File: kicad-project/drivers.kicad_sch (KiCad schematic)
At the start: 10 parts

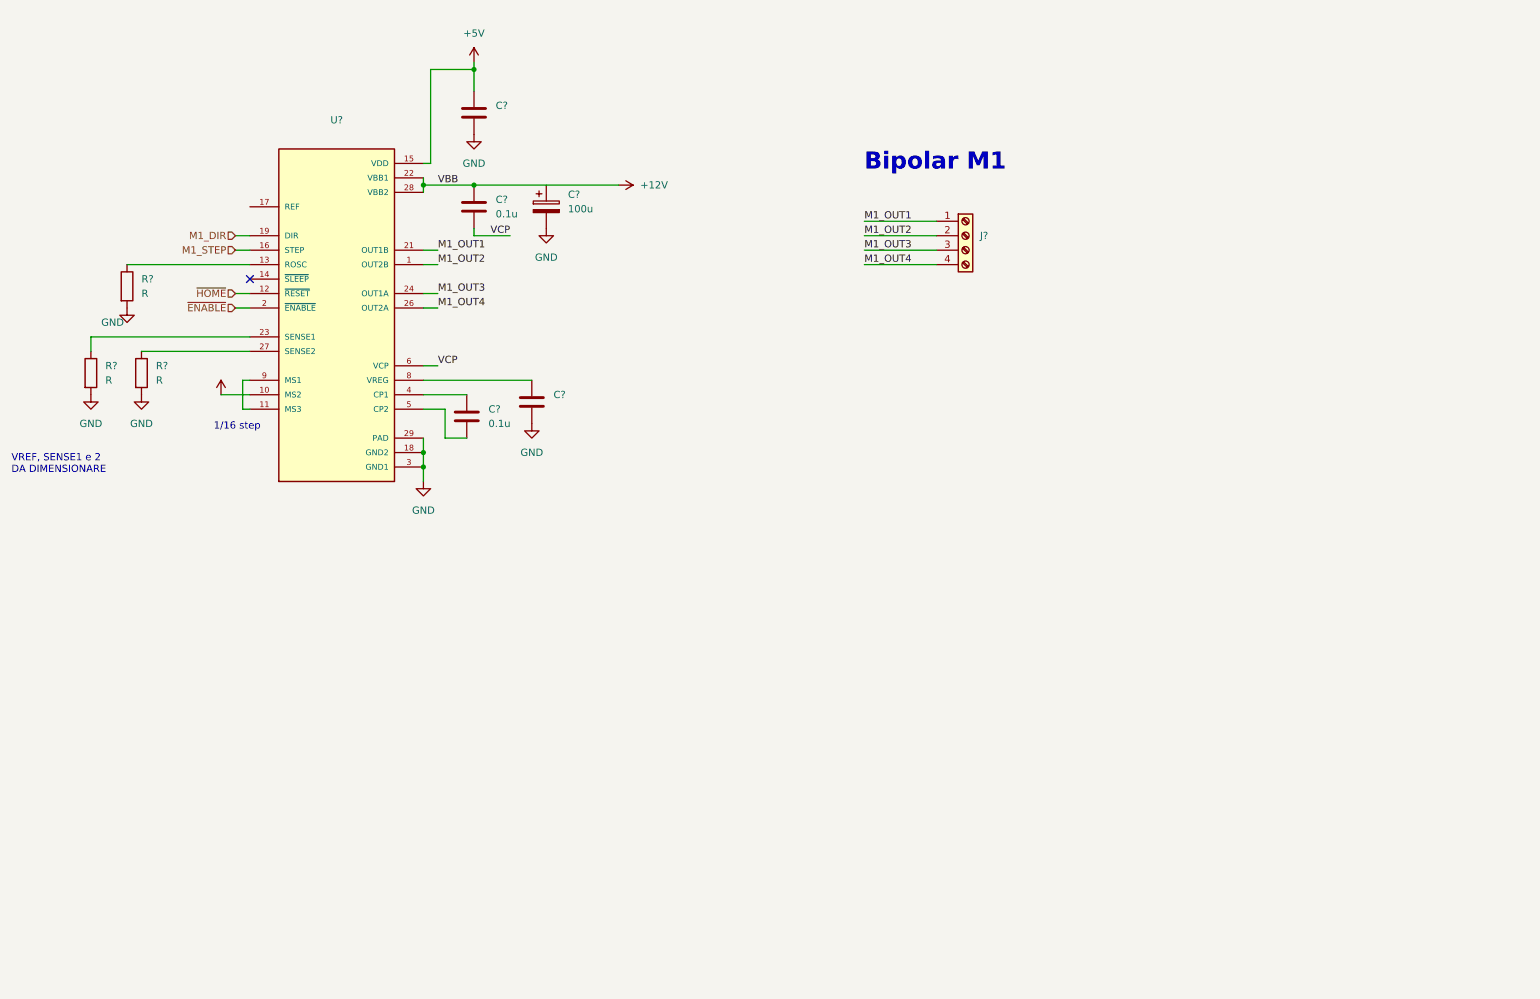
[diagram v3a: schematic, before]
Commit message: hw: add esp8266
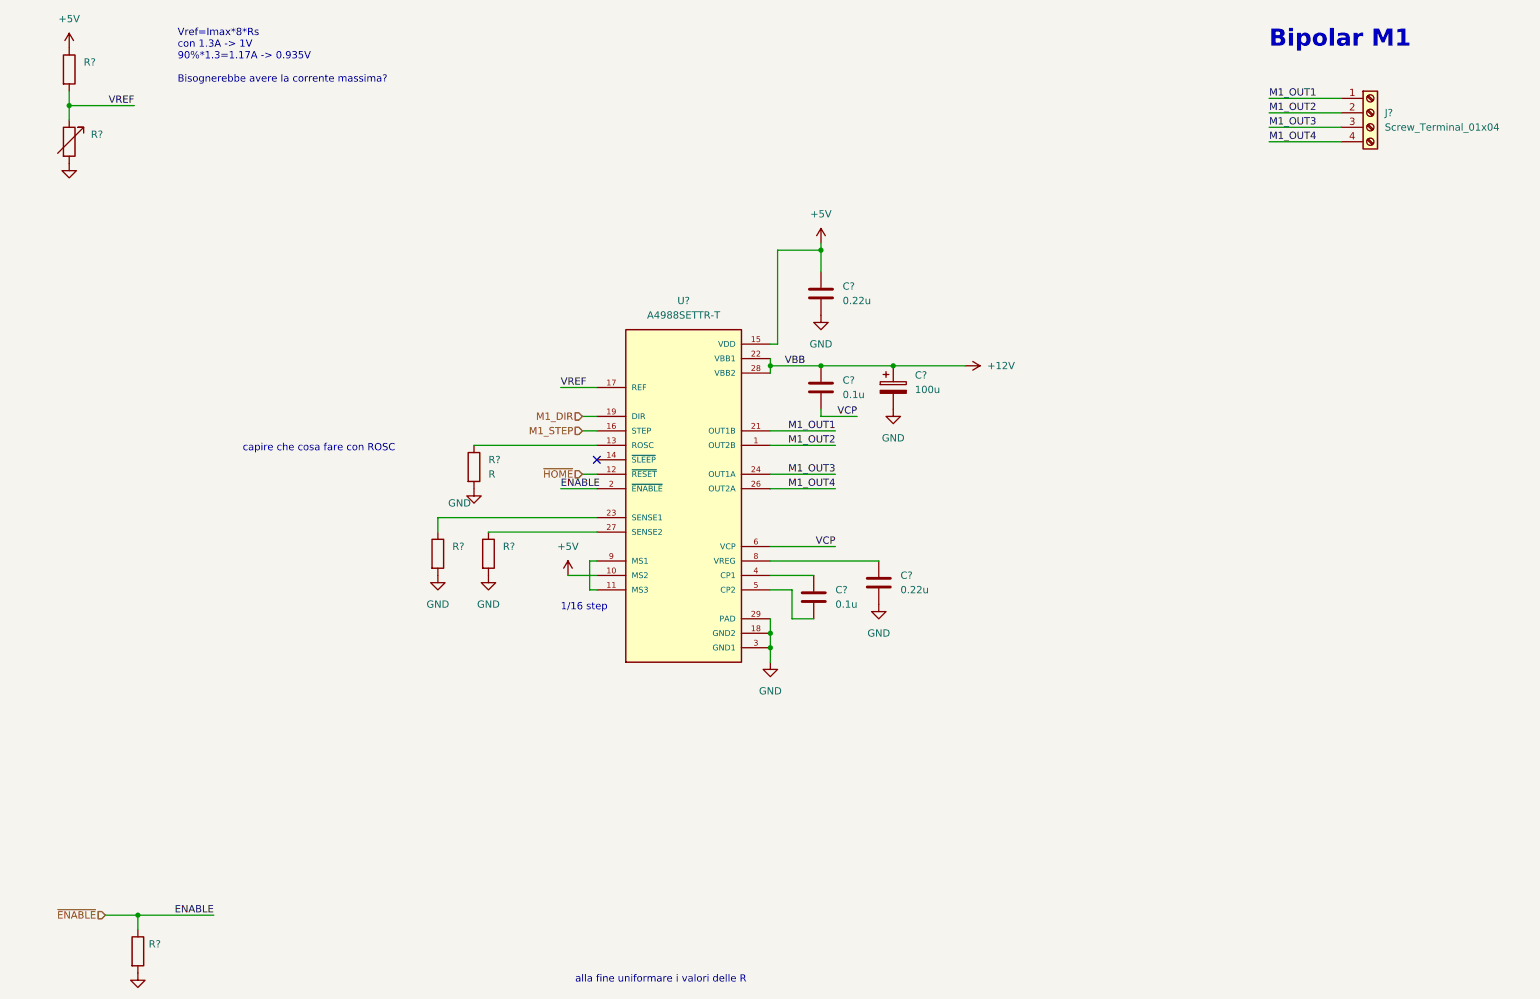
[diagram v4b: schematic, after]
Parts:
- added R? (x2): (no value), symbol Device:R
- added R?: (no value), symbol Device:R_Variable
- C? (x2): value (none) -> 0.22u
- J?: value (none) -> Screw_Terminal_01x04
- R? (x2): value R -> (none)
- U?: value (none) -> A4988SETTR-T; footprint (none) -> QFN50P500X500X90-29N
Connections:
- net +12V: now also C?.1
- net +5V: now also R?.1
- net GND: now also R?.2, R?.2
- net ~{ENABLE}: now also R?.1
- net VREF: now reaches U?.17 (REF)
- net VREF: now also R?.1, R?.2
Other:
- note added: "Vref=Imax*8*Rs con 1.3A -> 1V 90%*1.3=1.17A -> 0.935V Bisognerebbe avere la corrente massima?"
- note added: "alla fine uniformare i valori delle R"
- note added: "capire che cosa fare con ROSC"
- note removed: "VREF, SENSE1 e 2 DA DIMENSIONARE"
- moved on the sheet: C?, J?, R?, U?

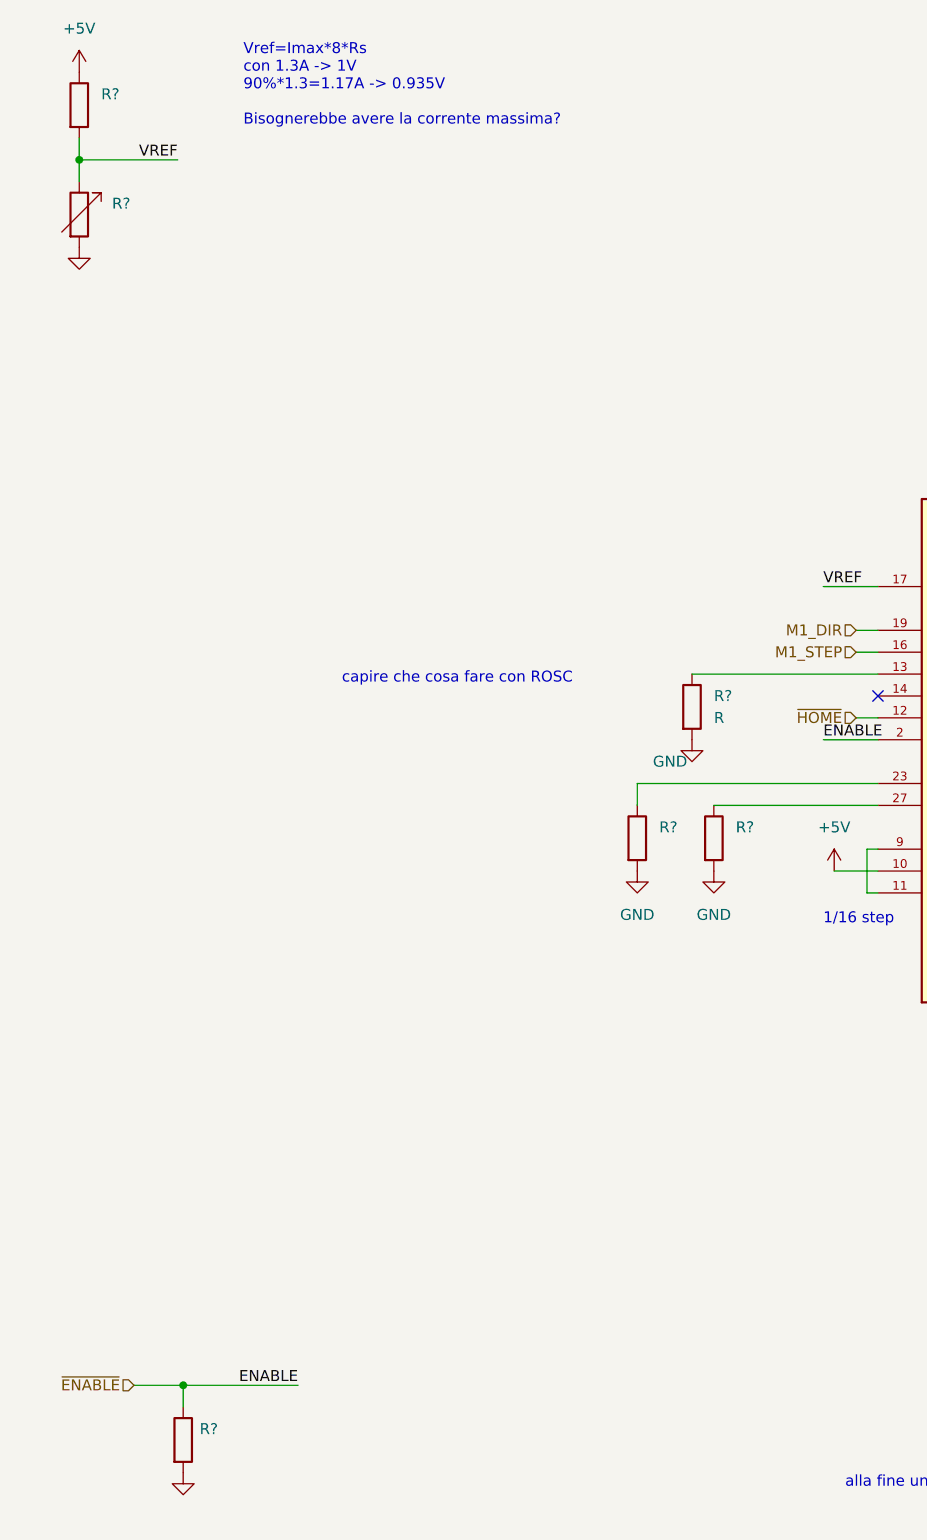
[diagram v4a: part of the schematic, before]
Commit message: hw: change to rp2040
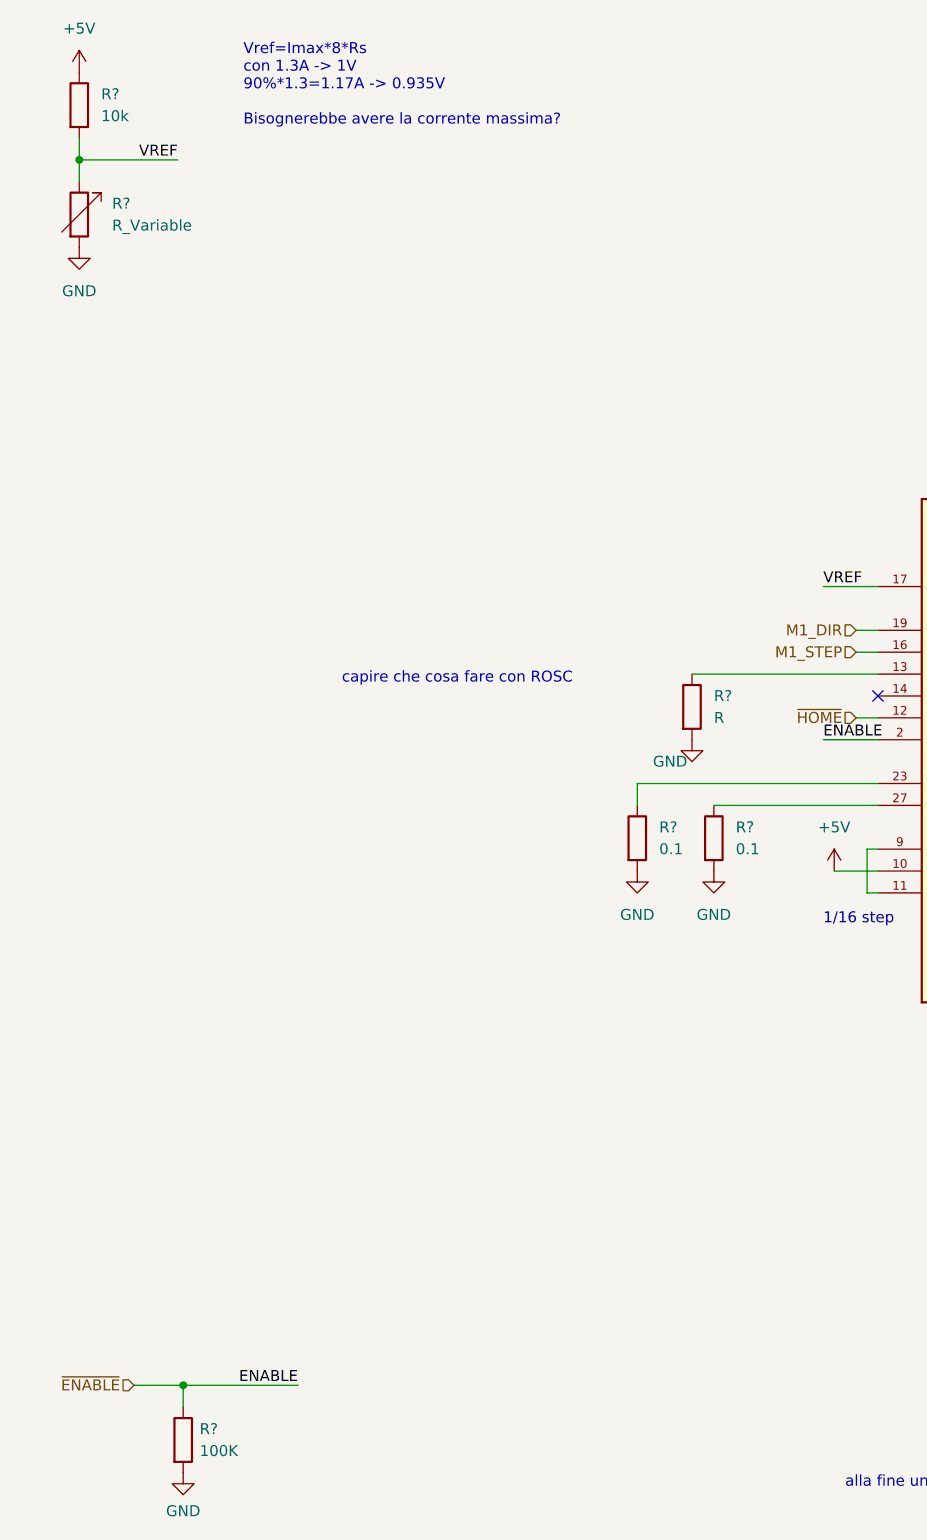
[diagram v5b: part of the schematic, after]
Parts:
- R?: value (none) -> 100K
- R?: value (none) -> R_Variable
- R? (x2): value (none) -> 0.1
- R?: value (none) -> 10k

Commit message: hw: change power management and drivers
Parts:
- removed J?: Screw_Terminal_01x04, TerminalBlock_TE-Connectivity:TerminalBlock_TE_282834-5_1x05_P2.54mm_Horizontal, symbol Connector:Screw_Terminal_01x04
- added C?: 100u, symbol Device:C_Polarized
- added J?: (no value), symbol Connector:Conn_01x04_Male
- added J? (x2): (no value), symbol Connector:Conn_01x08_Female
- R?: value R -> (none)
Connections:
- net GND: now also R?.1, C?.2; no longer R?.2
- net M1_OUT1: now also J?.1 (Pin_1)
- net M1_OUT2: now also U?.24 (OUT1A), J?.2 (Pin_2); no longer U?.1 (OUT2B)
- net M1_OUT3: now also U?.26 (OUT2A), J?.3 (Pin_3); no longer U?.24 (OUT1A)
- net M1_OUT4: now also U?.1 (OUT2B), J?.4 (Pin_4); no longer U?.26 (OUT2A)
- net at U?.13 (ROSC): now also R?.2; no longer R?.1
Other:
- note added: "Vref=Imax*8*Rs con 1.3A -> 1V 90%*1.3=1.17A -> 0.935V"
- note removed: "Vref=Imax*8*Rs con 1.3A -> 1V 90%*1.3=1.17A -> 0.935V Bisognerebbe avere la corrente massima?"
- note removed: "alla fine uniformare i valori delle R"
- note removed: "capire che cosa fare con ROSC"
- moved on the sheet: C?, R?, U?

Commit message: Bipolar pins
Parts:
- J?: value (none) -> Conn_01x04_Male
- J? (x2): value (none) -> Conn_01x08_Female
- R?: value (none) -> R
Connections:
- net +12V: now also C?.1, J?.8 (Pin_8)
- net GND: now also J?.1 (Pin_1), J?.7 (Pin_7)
- net M1_OUT1: no longer J?.1 (Pin_1)
- net M1_OUT2: no longer J?.2 (Pin_2)
- net M1_OUT3: no longer J?.3 (Pin_3)
- net M1_OUT4: no longer J?.4 (Pin_4)
- net +3V3: now reaches J?.2 (Pin_2)
- net +3V3: now also J?.2 (Pin_2), J?.3 (Pin_3), J?.4 (Pin_4)
- net MA_1B: now reaches J?.3 (Pin_3)
- net MA_1B: now also J?.4 (Pin_4)
- net MA_1A: now reaches J?.4 (Pin_4)
- net MA_1A: now also J?.3 (Pin_3)
- net MA_2A: now reaches J?.5 (Pin_5)
- net MA_2B: now reaches J?.6 (Pin_6)
- net MA_2B: now also J?.1 (Pin_1)
- net at J?.5 (Pin_5): now also J?.6 (Pin_6)
- net StepA: now reaches J?.7 (Pin_7)
- net DirA: now reaches J?.8 (Pin_8)
- new net M2_2A: J?.2 (Pin_2)
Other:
- note added: "Bipolar MA"
- note removed: "Bipolar M1"
- moved on the sheet: C?, J?
